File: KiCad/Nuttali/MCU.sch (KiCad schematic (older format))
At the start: 19 parts

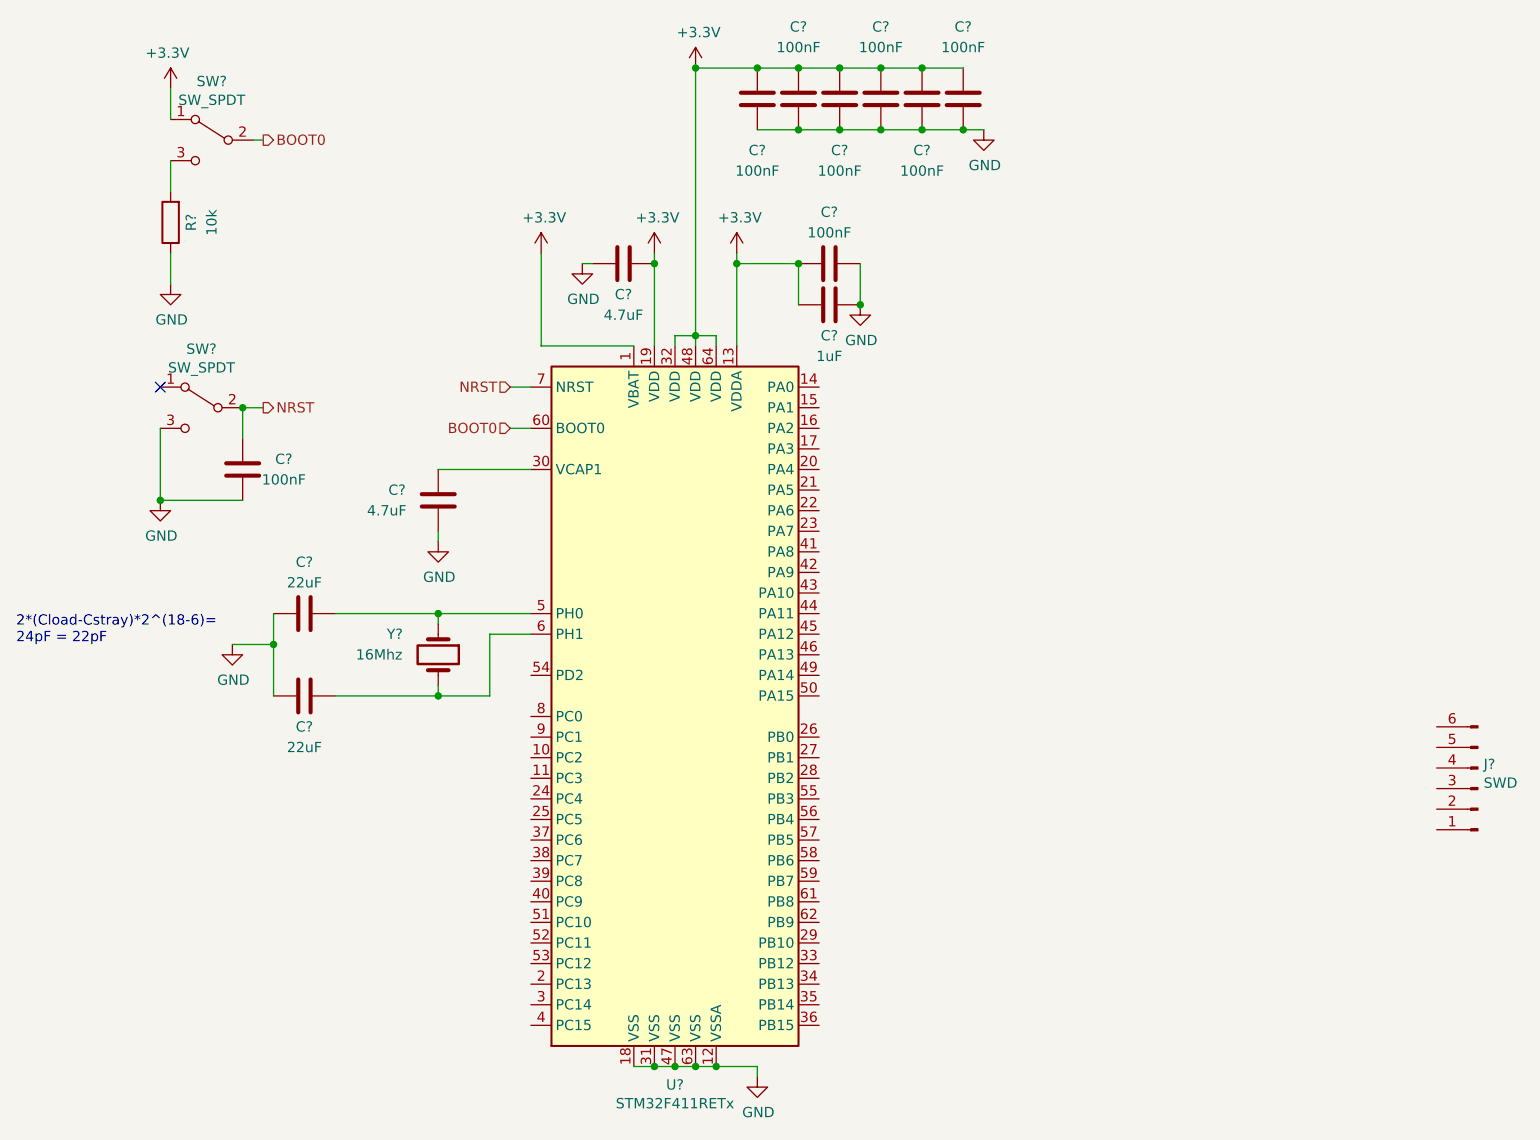
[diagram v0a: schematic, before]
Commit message: Fixed MCU
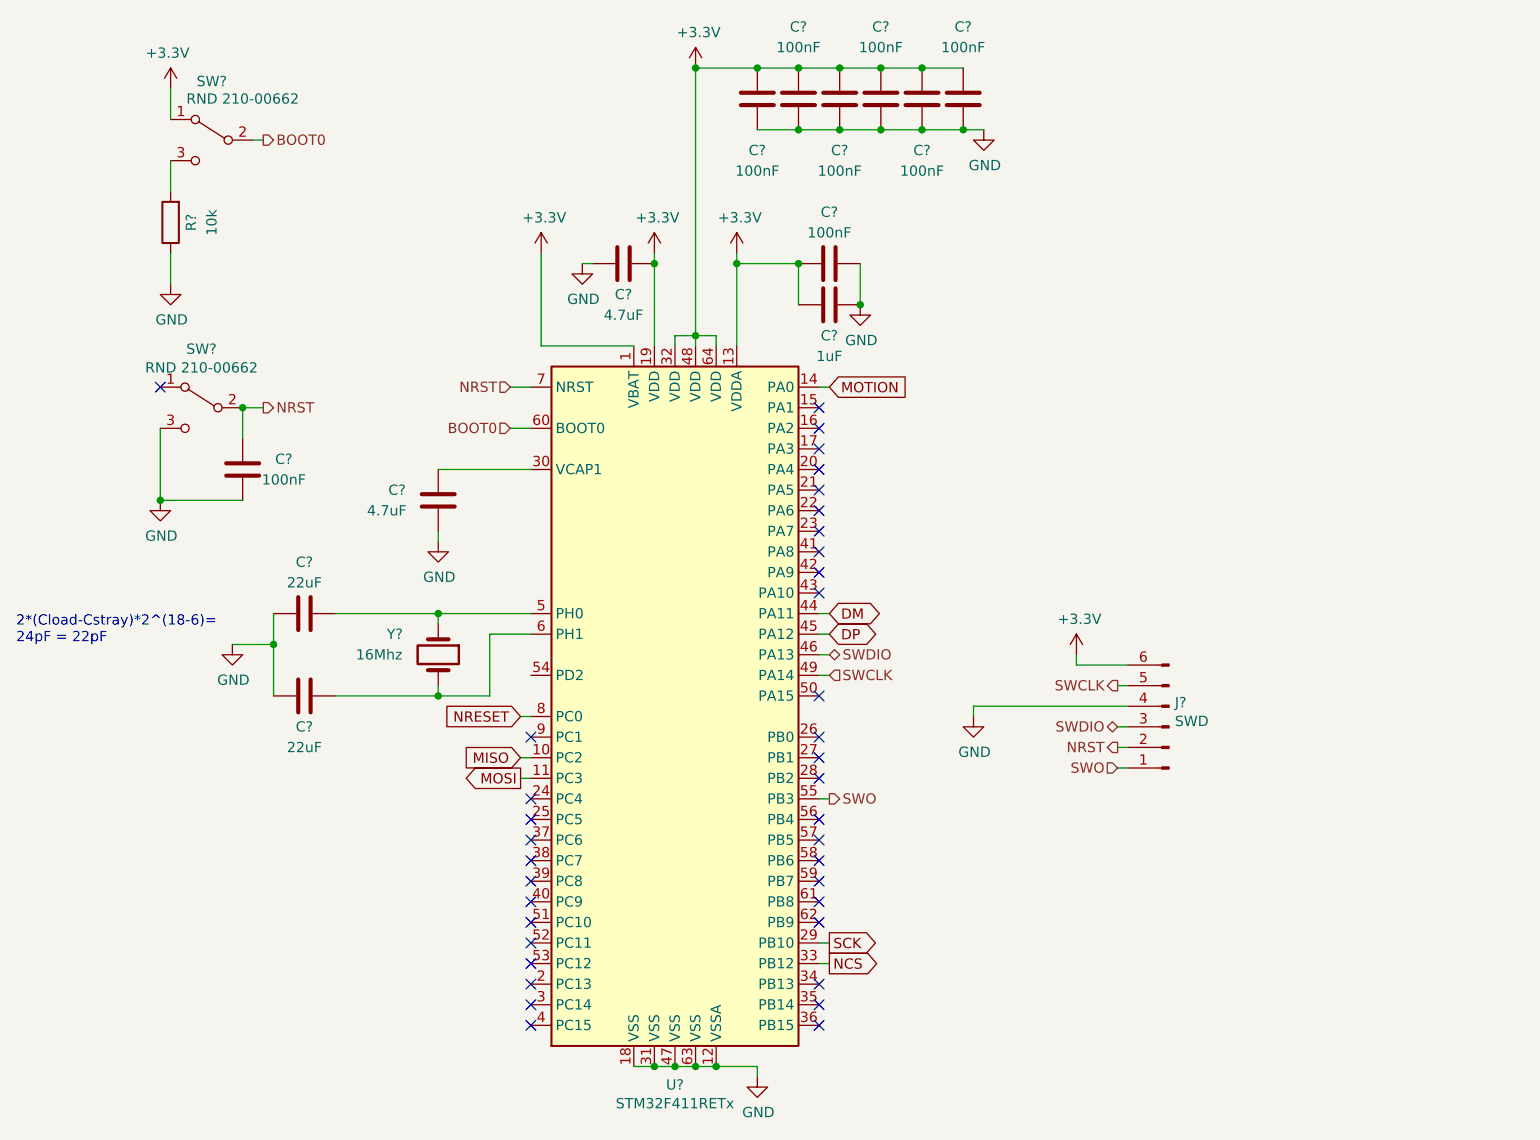
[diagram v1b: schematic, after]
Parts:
- SW? (x2): value SW_SPDT -> RND 210-00662
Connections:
- net +3V3: now also J?.6 (Pin_6)
- net GND: now also J?.4 (Pin_4)
- net NRST: now also J?.2 (Pin_2)
- net MISO: now reaches U?.10 (PC2)
- net MOSI: now reaches U?.11 (PC3)
- net MOTION: now reaches U?.14 (PA0)
- net SCK: now reaches U?.29 (PB10)
- net NCS: now reaches U?.33 (PB12)
- net DM: now reaches U?.44 (PA11)
- net DP: now reaches U?.45 (PA12)
- net SWDIO: now reaches U?.46 (PA13)
- net SWDIO: now also J?.3 (Pin_3)
- net SWCLK: now reaches U?.49 (PA14)
- net SWCLK: now also J?.5 (Pin_5)
- net SWO: now reaches U?.55 (PB3)
- net SWO: now also J?.1 (Pin_1)
- net NRESET: now reaches U?.8 (PC0)
- no-connect marks 1 -> 37
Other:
- moved on the sheet: J?
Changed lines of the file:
@@
 $Descr A4 11693 8268
 encoding utf-8
-Sheet 2 3
+Sheet 2 4
 Title ""
 Date ""
@@
 L Connector:Conn_01x06_Male J?
 U 1 1 602DCAE5
-P 9350 4600
-F 0 "J?" H 9322 4482 50  0000 R CNN
-F 1 "SWD" H 9322 4573 50  0000 R CNN
-F 2 "" H 9350 4600 50  0001 C CNN
-F 3 "~" H 9350 4600 50  0001 C CNN
-	1    9350 4600
+P 7850 4300
+F 0 "J?" H 7822 4182 50  0000 R CNN
+F 1 "SWD" H 7822 4273 50  0000 R CNN
+F 2 "" H 7850 4300 50  0001 C CNN
+F 3 "~" H 7850 4300 50  0001 C CNN
+	1    7850 4300
 	-1   0    0    1
 $EndComp
@@
 P 3200 1450
 F 0 "SW?" H 3200 1735 50  0000 C CNN
-F 1 "SW_SPDT" H 3200 1644 50  0000 C CNN
+F 1 "RND 210-00662" H 3050 1650 50  0000 C CNN
 F 2 "" H 3200 1450 50  0001 C CNN
 F 3 "~" H 3200 1450 50  0001 C CNN
@@
 P 3150 2750
 F 0 "SW?" H 3150 3035 50  0000 C CNN
-F 1 "SW_SPDT" H 3150 2944 50  0000 C CNN
+F 1 "RND 210-00662" H 3150 2944 50  0000 C CNN
 F 2 "" H 3150 2750 50  0001 C CNN
 F 3 "~" H 3150 2750 50  0001 C CNN
@@
 	1    0    0    -1
 $EndComp
+Text GLabel 4700 4250 0    50   Input ~ 0
+NRESET
+Wire Wire Line
+	4700 4250 4750 4250
+Wire Wire Line
+	4750 4450 4700 4450
+Wire Wire Line
+	4750 4550 4700 4550
+Text GLabel 4700 4450 0    50   Input ~ 0
+MISO
+Text GLabel 4700 4550 0    50   Output ~ 0
+MOSI
+Text GLabel 6200 2650 2    50   Input ~ 0
+MOTION
+Wire Wire Line
+	6200 2650 6150 2650
+Text GLabel 6200 3750 2    50   BiDi ~ 0
+DM
+Text GLabel 6200 3850 2    50   BiDi ~ 0
+DP
+Text GLabel 6200 5350 2    50   Output ~ 0
+SCK
+Text GLabel 6200 5450 2    50   Output ~ 0
+NCS
+Wire Wire Line
+	6200 5350 6150 5350
+Wire Wire Line
+	6200 5450 6150 5450
+Wire Wire Line
+	6200 4650 6150 4650
+Wire Wire Line
+	6200 4050 6150 4050
+Wire Wire Line
+	6200 3950 6150 3950
+Wire Wire Line
+	6200 3850 6150 3850
+Wire Wire Line
+	6200 3750 6150 3750
+Wire Wire Line
+	7650 4000 7400 4000
+Wire Wire Line
+	7400 4000 7400 3950
+$Comp
+L power:+3.3V #PWR?
+U 1 1 601F634D
+P 7400 3950
+F 0 "#PWR?" H 7400 3800 50  0001 C CNN
+F 1 "+3.3V" H 7415 4123 50  0000 C CNN
+F 2 "" H 7400 3950 50  0001 C CNN
+F 3 "" H 7400 3950 50  0001 C CNN
+	1    7400 3950
+	1    0    0    -1
+$EndComp
+$Comp
+L power:GND #PWR?
+U 1 1 601F695B
+P 6900 4250
+F 0 "#PWR?" H 6900 4000 50  0001 C CNN
+F 1 "GND" H 6905 4077 50  0000 C CNN
+F 2 "" H 6900 4250 50  0001 C CNN
+F 3 "" H 6900 4250 50  0001 C CNN
+	1    6900 4250
+	1    0    0    -1
+$EndComp
+Wire Wire Line
+	6900 4200 7650 4200
+Wire Wire Line
+	6900 4250 6900 4200
+Text HLabel 7600 4400 0    50   Output ~ 0
+NRST
+Text HLabel 6200 4650 2    50   Output ~ 0
+SWO
+Text HLabel 7600 4500 0    50   Input ~ 0
+SWO
+Wire Wire Line
+	7600 4500 7650 4500
+Wire Wire Line
+	7650 4400 7600 4400
+Text HLabel 6200 3950 2    50   BiDi ~ 0
+SWDIO
+Text HLabel 7600 4300 0    50   BiDi ~ 0
+SWDIO
+Text HLabel 6200 4050 2    50   Input ~ 0
+SWCLK
+Text HLabel 7600 4100 0    50   Output ~ 0
+SWCLK
+Wire Wire Line
+	7600 4100 7650 4100
+Wire Wire Line
+	7600 4300 7650 4300
+NoConn ~ 6150 2750
+NoConn ~ 6150 2850
+NoConn ~ 6150 2950
+NoConn ~ 6150 3050
+NoConn ~ 6150 3150
+NoConn ~ 6150 3250
+NoConn ~ 6150 3350
+NoConn ~ 6150 3450
+NoConn ~ 6150 3550
+NoConn ~ 6150 3650
+NoConn ~ 6150 4150
+NoConn ~ 6150 4350
+NoConn ~ 6150 4450
+NoConn ~ 6150 4550
+NoConn ~ 6150 4750
+NoConn ~ 6150 4850
+NoConn ~ 6150 4950
+NoConn ~ 6150 5050
+NoConn ~ 6150 5150
+NoConn ~ 6150 5250
+NoConn ~ 6150 5550
+NoConn ~ 6150 5650
+NoConn ~ 6150 5750
+NoConn ~ 4750 5750
+NoConn ~ 4750 5650
+NoConn ~ 4750 5550
+NoConn ~ 4750 5450
+NoConn ~ 4750 5350
+NoConn ~ 4750 5250
+NoConn ~ 4750 5150
+NoConn ~ 4750 5050
+NoConn ~ 4750 4950
+NoConn ~ 4750 4850
+NoConn ~ 4750 4750
+NoConn ~ 4750 4650
+NoConn ~ 4750 4350
 $EndSCHEMATC

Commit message: Fixed power and USB
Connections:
- net DM renamed D-
- net DP renamed D+
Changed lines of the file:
@@
 	6200 2650 6150 2650
 Text GLabel 6200 3750 2    50   BiDi ~ 0
-DM
+D-
 Text GLabel 6200 3850 2    50   BiDi ~ 0
-DP
+D+
 Text GLabel 6200 5350 2    50   Output ~ 0
 SCK
